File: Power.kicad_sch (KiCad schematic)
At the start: 81 parts, among them U1 ZXCT1009F, U2 LT1763, U3 TPS62110, U30 PTN78020A, U31 LT3097, U5 LT1763, U6 TPS62110

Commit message: Updated Channel 1 and fixes from review
Updated Channel 1 to use the INA851.
Fixed the ORNTA part pinout.
Fixed feedback on LT1763s.
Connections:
- net VDD1P8V: now also C19.1, U2.5 (SENSE)
- net VSS3P3V: now also C15.1, U5.5 (SENSE)
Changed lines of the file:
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@@
   (junction (at 328.93 129.54) (diameter 0) (color 0 0 0 0)
   )
+  (junction (at 360.68 116.84) (diameter 0) (color 0 0 0 0)
+  )
   (junction (at 292.1 116.84) (diameter 0) (color 0 0 0 0)
   )
+  (junction (at 351.79 76.2) (diameter 0) (color 0 0 0 0)
+  )
   (junction (at 294.64 220.98) (diameter 0) (color 0 0 0 0)
   )
@@
   (junction (at 320.04 82.55) (diameter 0) (color 0 0 0 0)
   )
+  (junction (at 351.79 69.85) (diameter 0) (color 0 0 0 0)
+  )
   (junction (at 201.93 224.79) (diameter 0) (color 0 0 0 0)
   )
@@
   (junction (at 181.61 224.79) (diameter 0) (color 0 0 0 0)
   )
+  (junction (at 360.68 123.19) (diameter 0) (color 0 0 0 0)
+  )
   (junction (at 302.26 53.34) (diameter 0) (color 0 0 0 0)
   )
@@
     (stroke (width 0) (type default))
   )
+  (wire (pts (xy 351.79 69.85) (xy 368.3 69.85))
+    (stroke (width 0) (type default))
+  )
   (wire (pts (xy 274.32 100.33) (xy 274.32 104.14))
     (stroke (width 0) (type default))
@@
     (stroke (width 0) (type default))
   )
+  (wire (pts (xy 360.68 116.84) (xy 360.68 123.19))
+    (stroke (width 0) (type default))
+  )
   (wire (pts (xy 78.74 143.51) (xy 78.74 154.94))
     (stroke (width 0) (type default))
@@
     (stroke (width 0) (type default))
   )
+  (wire (pts (xy 360.68 116.84) (xy 377.19 116.84))
+    (stroke (width 0) (type default))
+  )
   (wire (pts (xy 201.93 198.12) (xy 78.74 198.12))
     (stroke (width 0) (type default))
@@
     (stroke (width 0) (type default))
   )
-  (wire (pts (xy 358.14 116.84) (xy 377.19 116.84))
+  (wire (pts (xy 358.14 116.84) (xy 360.68 116.84))
     (stroke (width 0) (type default))
   )
@@
     (stroke (width 0) (type default))
   )
+  (wire (pts (xy 351.79 69.85) (xy 351.79 76.2))
+    (stroke (width 0) (type default))
+  )
   (wire (pts (xy 213.36 200.66) (xy 213.36 203.2))
     (stroke (width 0) (type default))
@@
     (stroke (width 0) (type default))
   )
-  (wire (pts (xy 349.25 69.85) (xy 368.3 69.85))
-    (stroke (width 0) (type default))
-  )
+  (wire (pts (xy 349.25 69.85) (xy 351.79 69.85))
+    (stroke (width 0) (type default))
+  )

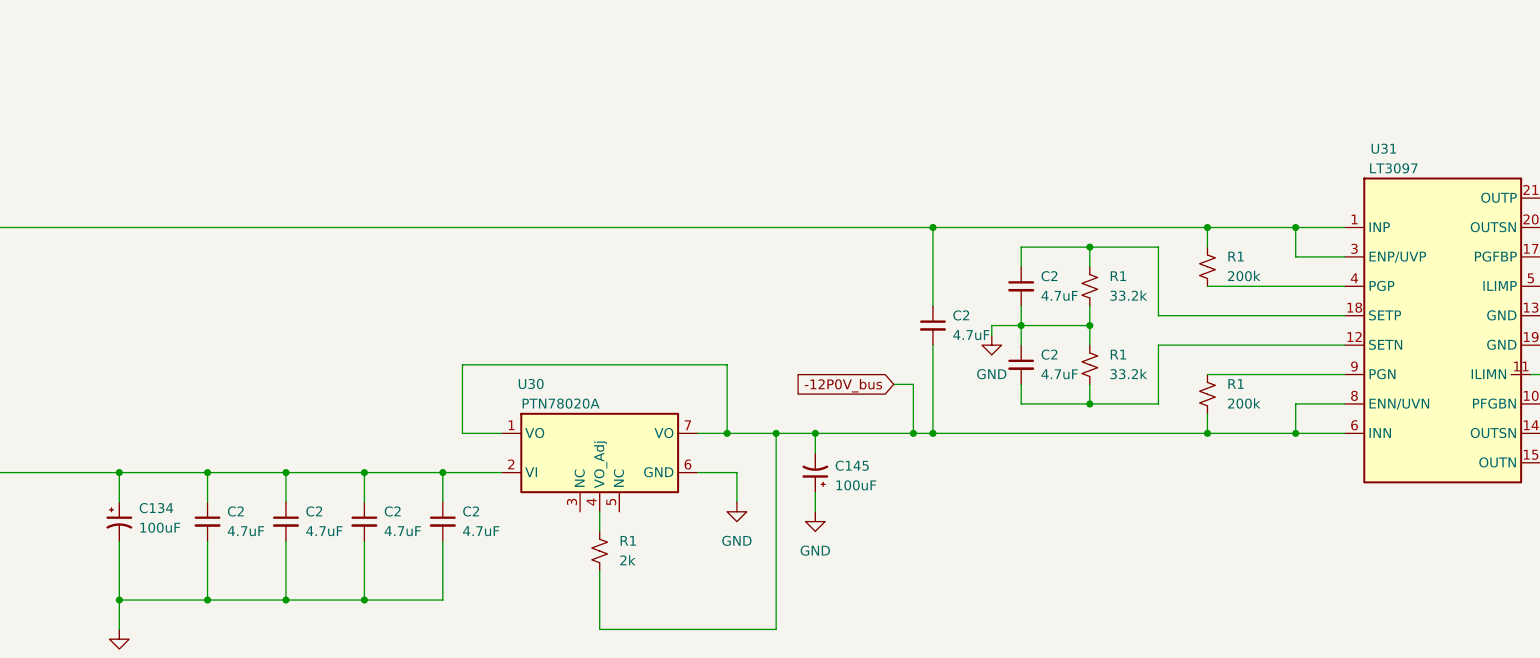
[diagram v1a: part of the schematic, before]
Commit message: Schmatic Updates
Updated:
ADC MCLK signal
Removed PMOD connectors
Added Coax input for iRIG signal with 5V buffer
Moved around FMC pin mapping
Changed relay driver chip daisy chain order
Changed all input AFE to new design based around the INA851 chip
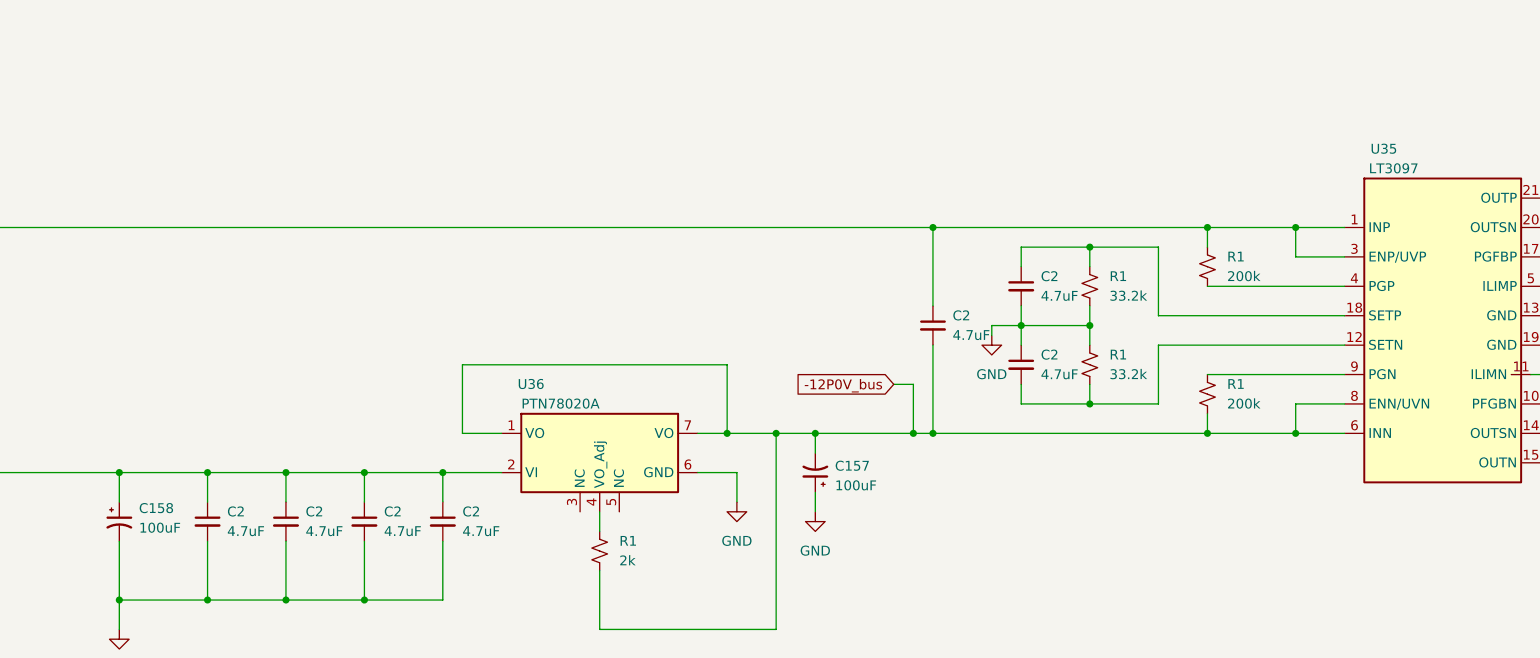
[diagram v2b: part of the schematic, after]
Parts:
- renumbered C145 to C157, C134 to C158, U31 to U35, U30 to U36

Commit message: Updated Schematics
Changes:
-Moved Input resistors to after Coupling Relay
-Added diff cap at ADC input
-Changed the ADC clocking configuration (added quad LVDS driver)
-Changed some signal names for consistancy
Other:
- note added: "NEEDS REVISION TO Change AFE POWER RAILS"
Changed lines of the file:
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@@
     (stroke (width 0) (type default))
+  )
+  (text "NEEDS REVISION TO Change AFE POWER RAILS" (at 29.21 217.17 0)
+    (effects (font (size 10 10) (thickness 2) bold) (justify left bottom))
   )
   (global_label "V12P0V_bus" (shape input) (at 111.76 54.61 0) (fields_autoplaced)

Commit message: Updated Schematics with latest suggestions
updates:
-Revised Power supply section
-Changed clock buffer chip for ADC Clock
- Added additional no pop & jumper parts for board debugging
-Other small part changes
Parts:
- removed C11: 10pF, symbol Device:C_Small
- removed C12, C13: 47uF, symbol Device:C_Small
- removed C14, C3: 1uF, symbol Device:C_Small
- removed C15: 10nF, symbol Device:C_Small
- removed C157, C158: 100uF, symbol Device:C_Polarized_Small_US
- removed C16: 10uF, symbol Device:C_Small
- removed C2 (x4): 4.7uF, symbol Device:C_Small
- removed C4, C5: 22uF, symbol Device:C_Small
- removed J5: ~, symbol Custom_Lib_MPEX_Zest:CONN_U-FL_SMD
- removed L1, L5: 600, symbol Device:L_Small
- removed L3: 10uH, symbol Device:L_Small
- removed R1: 2k, symbol Device:R_Small_US
- removed R14, R15, R16: 422k, symbol Device:R_Small_US
- removed R23, R24: 4.75k, symbol Device:R_Small_US
- removed R7, R8, R9: 11.5k, symbol Device:R_Small_US
- removed U36: PTN78020A, symbol AD7768_Digitizer_SLib:PTN78020A
- removed U5: LT1763, symbol Custom_Lib_MPEX_Zest:LT1763_12pin
- removed U6: TPS62110, symbol Custom_Lib_MPEX_Zest:TPS62110
- added C16 (x5), C2: 10uF, symbol Device:C_Small
- added C2: 2.2uF, symbol Device:C_Small
- added C2: 22uF, symbol Device:C_Small
- added C7: 1uF, symbol Device:C_Small
- added C? (x4): 100nF, Capacitor_SMD:C_0603_1608Metric, symbol Device:C_Small
- added C?: 4.7nF, Capacitor_SMD:C_0603_1608Metric, symbol Device:C_Small
- added C?: 2.2nF, Capacitor_SMD:C_0603_1608Metric, symbol Device:C_Small
- added D1 (x2): PD3S230H, symbol Device:D_Zener
- added J4 (x2): ~, symbol Custom_Lib_MPEX_Zest:CONN_U-FL_SMD
- added L3901: 6.8uH, symbol Device:L
- added L3902: 15uH, symbol Device:L_Coupled
- added L3903: 2.2uH, symbol Device:L
- added Q3901: FDMC510P, symbol Simulation_SPICE:PMOS
- added R1 (x2): 53.6k, symbol Device:R_Small_US
- added R1: 6.49k, symbol Device:R_Small_US
- added R1 (x2): 215k, symbol Device:R_Small_US
- added R1 (x2): 165k, symbol Device:R_Small_US
- added R1 (x2): 100k, symbol Device:R_Small_US
- added R1: 180k, symbol Device:R_Small_US
- added R1: 14.7k, symbol Device:R_Small_US
- added U3901: LT8582, symbol AD7768_Digitizer_SLib:LT8582
- added U3902: TPS62163DSG, Package_SON:WSON-8-1EP_2x2mm_P0.5mm_EP0.9x1.6mm_ThermalVias, symbol Regulator_Switching:TPS62163DSG
- R10: value 11.5k -> 100k
- U3: MPN (none) -> TPS62110
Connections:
- net GND: now also U3.1 (PGND), U3.11 (GND), U3.12 (GND), U3.16 (PGND), U3.5 (SYNC), U3.7 (LBI), U3.9 (AGND), U3.PAD (PwPD), C16.1, C16.2, C16.2, C16.2, C16.2, C2.2, C2.2, C7.2, C?.1, C?.2, C?.2, C?.2, C?.2, C?.2, D1.1 (K), J4.2, J4.2, J4.3, J4.3, R1.1, R1.1, U3901.19 (SYNC1), U3901.25 (GND), U3902.1 (PGND), U3902.4 (AGND), U3902.5 (FB), U3902.9 (PAD)
- net V12P0V_bus: now also C16.1, C16.1, C2.1, L3901.1, L3902.1, R1.1, R1.1, R1.1, R1.1, U3901.11 (Vin2), U3901.2 (Vin1), U3902.2 (VIN), U3902.3 (EN); no longer C2.1, R1.1, U35.1 (INP), U35.3 (ENP/UVP)
- net +5V: now reaches R10.1
- net +5V: now also C2.1, L3903.2, U3902.6 (VOS); no longer U3.5 (SYNC)
- net +10V renamed 14V+
- net -10V renamed 14V-
- net -12P0V_bus renamed -15V
- net -15V: now also C16.2, J4.1, L3902.3, R1.2
- net PWR_EN: no longer names the net of U3.4 (EN)
- net PWR_EN: now also C6.1, C7.1, C8.1, L2.2, U3.2 (VIN), U3.3 (VIN), U3.8 (VINA), C7.1
- removed net PWR_SYNC: C6.1, C7.1, C8.1, L2.2, R10.2, U3.2 (VIN), U3.3 (VIN), U3.8 (VINA)
- net V3P7V_Mon renamed 2P3V_Mon
- new net: C?.2, U3901.17 (SS2)
- new net: R1.2, U3901.21 (RT1)
- new net: C2.1, L3902.2, U3901.12 (SWA2), U3901.13 (SWB2)
- new net: C2.2, D1.2 (A), L3902.4
- new net: C?.1, R1.2, U3901.5 (Vc1)
- new net: Q3901.2 (G), R1.1, U3901.4 (GATE1)
- new net: C16.1, D1.1 (K), Q3901.3 (S), R1.2, R1.2
- new net: C?.1, R1.1 (x2)
- new net: R1.2, U3901.16 (RT2)
- new net: R1.2, U3901.22 (~{SHDN1})
- new net: R10.2, U3902.8 (PG)
- new net: R1.2, U3901.15 (~{SHDN2})
- new net: L3903.1, U3902.7 (SW)
- new net: R1.1, U3901.6 (FBX1)
- new net: R1.2, U3901.10 (PG2)
- new net: C?.1, R1.2, U3901.8 (Vc2)
- new net: R1.1, U3901.7 (FBX2)
- new net: R1.2, U3901.3 (PG1)
- new net: D1.2 (A), L3901.2, U3901.1 (SWA1), U3901.24 (SWB1)
- new net: U3901.18 (SYNC2), U3901.23 (CLKOUT1)
- new net: C?.1, U3901.20 (SS1)
- new net 15V: C16.1, C2.1, J4.1, Q3901.1 (D), R1.1, U35.1 (INP), U35.3 (ENP/UVP)
- no-connect marks 0 -> 1
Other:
- note removed: "NEEDS REVISION TO Change AFE POWER RAILS"
- moved on the sheet: C10, C17, C18, C19, C2, C20, C21, C6, C7, C8, C9, D1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

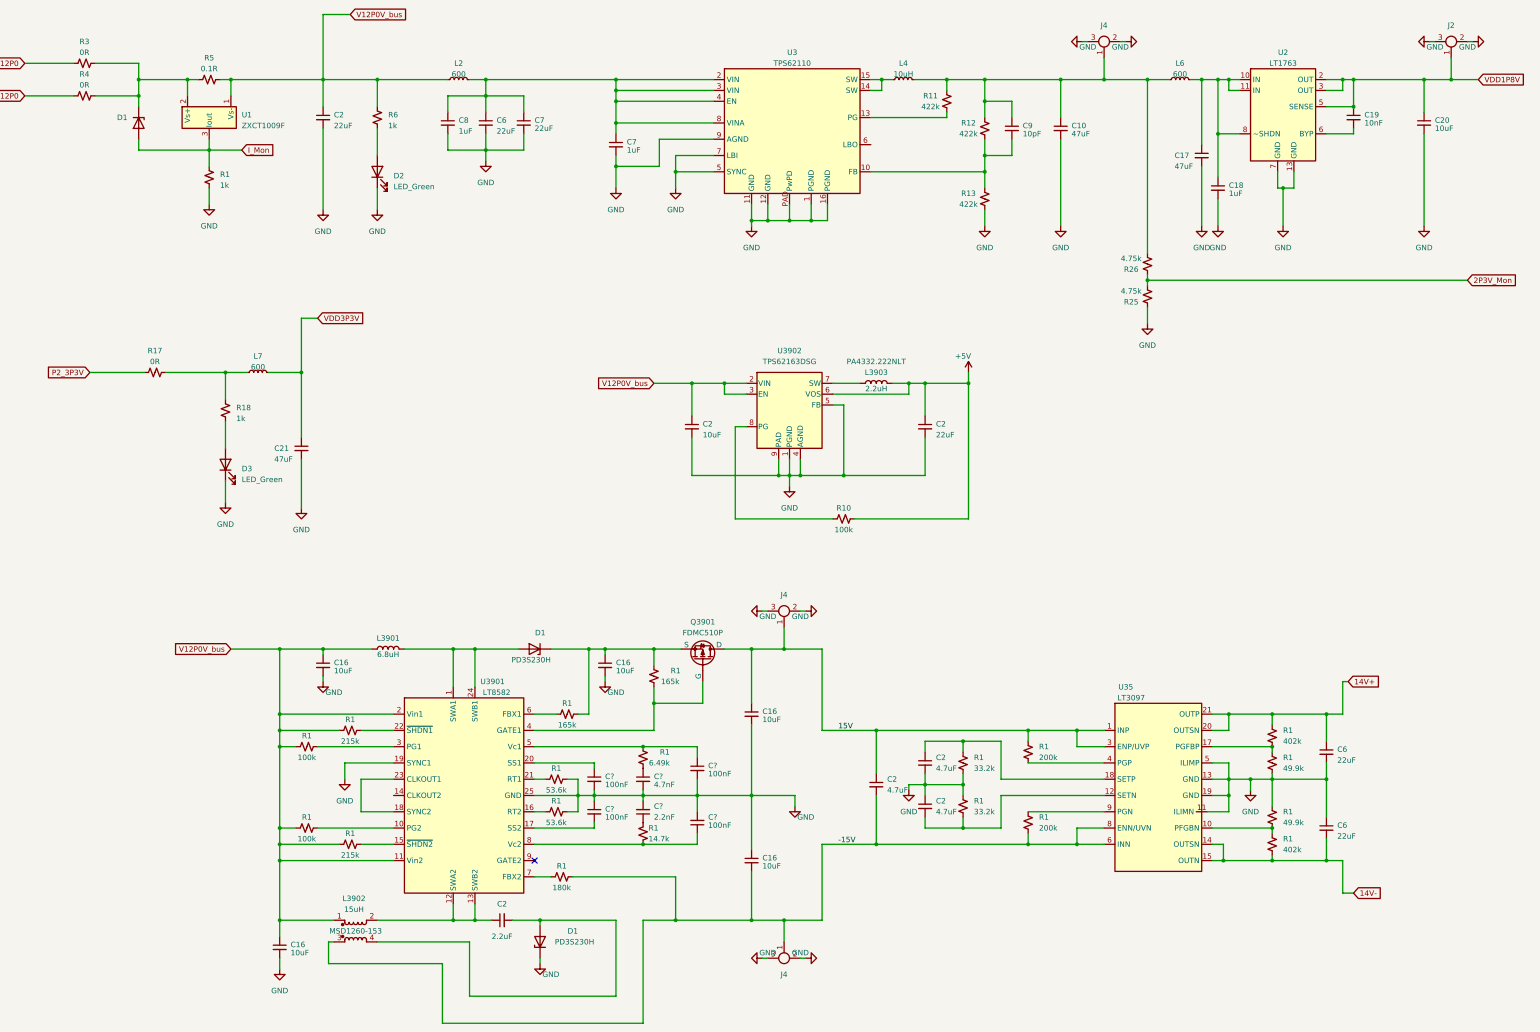
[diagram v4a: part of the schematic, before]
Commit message: Schematic Updates
Updated:
-Fixed AMC7823 labels
-Added present detect signals on FMC
-Added ferrite beads in Power Section and AFE
-Added 0R in power section
-Revised EEPROM connections
-Changed +5V SMPS part to one with an integrated inductor
-Added more detail on FMC connector
-Added file showing SMPS calculations
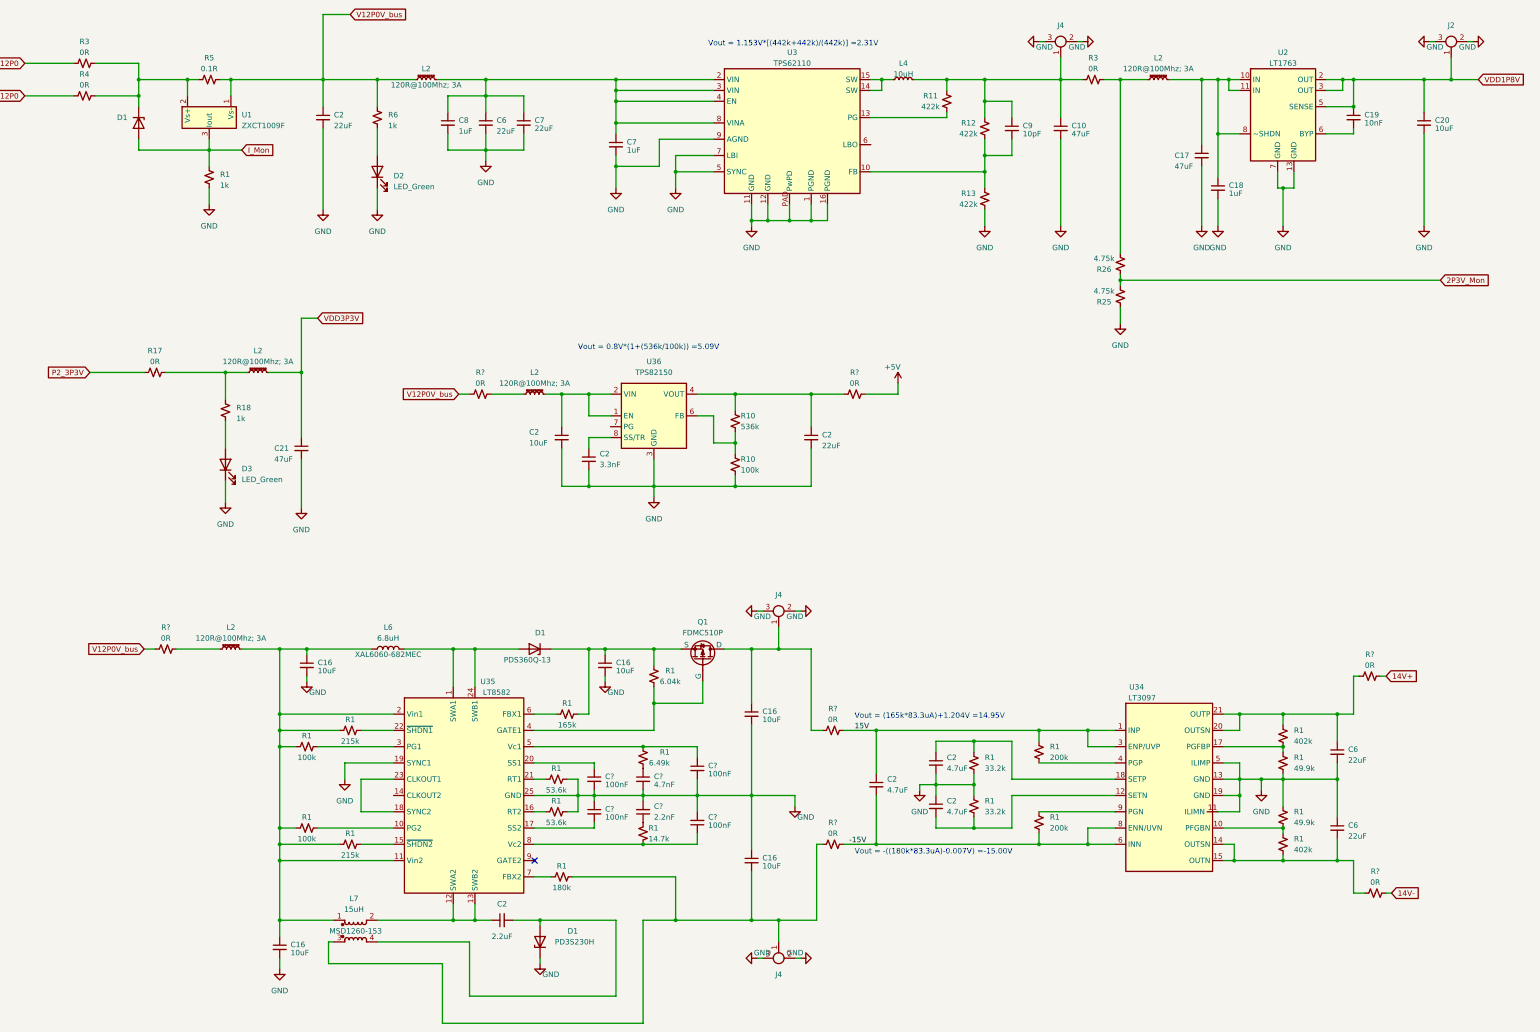
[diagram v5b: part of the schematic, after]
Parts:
- removed L3903: 2.2uH, symbol Device:L
- removed L6, L7: 600, symbol Device:L_Small
- removed U3902: TPS62163DSG, Package_SON:WSON-8-1EP_2x2mm_P0.5mm_EP0.9x1.6mm_ThermalVias, symbol Regulator_Switching:TPS62163DSG
- added C2: 3.3nF, symbol Device:C_Small
- added L2 (x4): 120R@100Mhz; 3A, symbol Device:L_Ferrite_Small
- added R10: 100k, symbol Device:R_Small_US
- added R3: 0R, symbol Device:R_Small_US
- added R? (x7): 0R, Capacitor_SMD:C_0603_1608Metric, symbol Device:R_Small_US
- added U36: TPS82150, Package_LGA:Texas_MicroSiP-8-1EP_2.8x3.0mm_P0.65mm_EP1.1x1.9mm_SMD_ThermalVias, symbol Regulator_Switching:TPS82150
- C2: MPN (none) -> GCJ31CR71H225KA12L; Note X5R 25V 1206 -> X5R 50V 1206
- D1: value PD3S230H -> PDS360Q-13; MPN (none) -> PDS360Q-13
- L2: value 600 -> 120R@100Mhz; 3A; symbol Device:L_Small -> Device:L_Ferrite_Small; MPN (none) -> BLM18KG121TN1D
- L6: renamed from L3901; MPN (none) -> XAL6060-682MEC
- R1: value 165k -> 6.04k
- R10: value 100k -> 536k
- U1: MPN (none) -> ZXCT1009F
- renumbered L3902 to L7, Q3901 to Q1, U35 to U34, U3901 to U35
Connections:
- net +5V: now also R?.2; no longer C2.1, R10.1
- net -15V: now also R?.2; no longer C16.2, J4.1, L7.3, R1.2
- net 14V+: now also R?.2; no longer C6.1, R1.1, U34.20 (OUTSN), U34.21 (OUTP)
- net 14V-: now also R?.2; no longer C6.2, R1.2, U34.14 (OUTSN), U34.15 (OUTN)
- net 15V: now also R?.2; no longer C16.1, J4.1, Q1.1 (D)
- net GND: now also C2.2, R10.2, U36.3 (GND), U36.9 (GND)
- net V12P0V_bus: now also R?.1, R?.1; no longer C16.1, C16.1, C2.1, L6.1, L7.1, R1.1, R1.1, R1.1, R1.1, U35.11 (Vin2), U35.2 (Vin1)
- net VDD3P3V: now also L2.2
- net at C10.1, C9.1, J4.1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: now also R3.1; no longer R26.2
- net at C17.1, C18.1, U2.10 (IN)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: now also L2.2
- net at R17.2, R18.2: now also L2.1
- net at R10.2: now also R10.1, U36.6 (FB)
- new net: C16.1, J4.1, Q1.1 (D), R?.1
- new net: C2.1, U36.8 (SS/TR)
- new net: C6.2, R1.2, R?.1, U34.14 (OUTSN), U34.15 (OUTN)
- new net: C6.1, R1.1, R?.1, U34.20 (OUTSN), U34.21 (OUTP)
- new net: C16.2, J4.1, L7.3, R1.2, R?.1
- new net: L2.1, R26.2, R3.2
- new net: C2.1, R10.1, R?.1, U36.4 (VOUT), U36.5 (VOUT)
- new net: C16.1, C16.1, L2.2, L6.1, L7.1, R1.1, R1.1, R1.1, R1.1, U35.11 (Vin2), U35.2 (Vin1)
- new net: C2.1, L2.2, U36.1 (EN), U36.2 (VIN)
- new net: L2.1, R?.2 (x2)
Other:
- note added: "Vout = (165k*83.3uA)+1.204V =14.95V"
- note added: "Vout = -((180k*83.3uA)-0.007V) =-15.00V"
- note added: "Vout = 0.8V*(1+(536k/100k)) =5.09V"
- note added: "Vout = 1.153V*[(442k+442k)/(442k)] =2.31V"
- moved on the sheet: C16, C2, C6, J4, R1, R10, R25, R26, U34
